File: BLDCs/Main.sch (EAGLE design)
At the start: 60 parts, among them IC1 MEGA8-AI, IC3 TP4056, J1 PIC_ICSP_MINI_5_PIN, U4 LM1117 3.3, X1 MINI-USB-32005-201, Y1 16MHZ

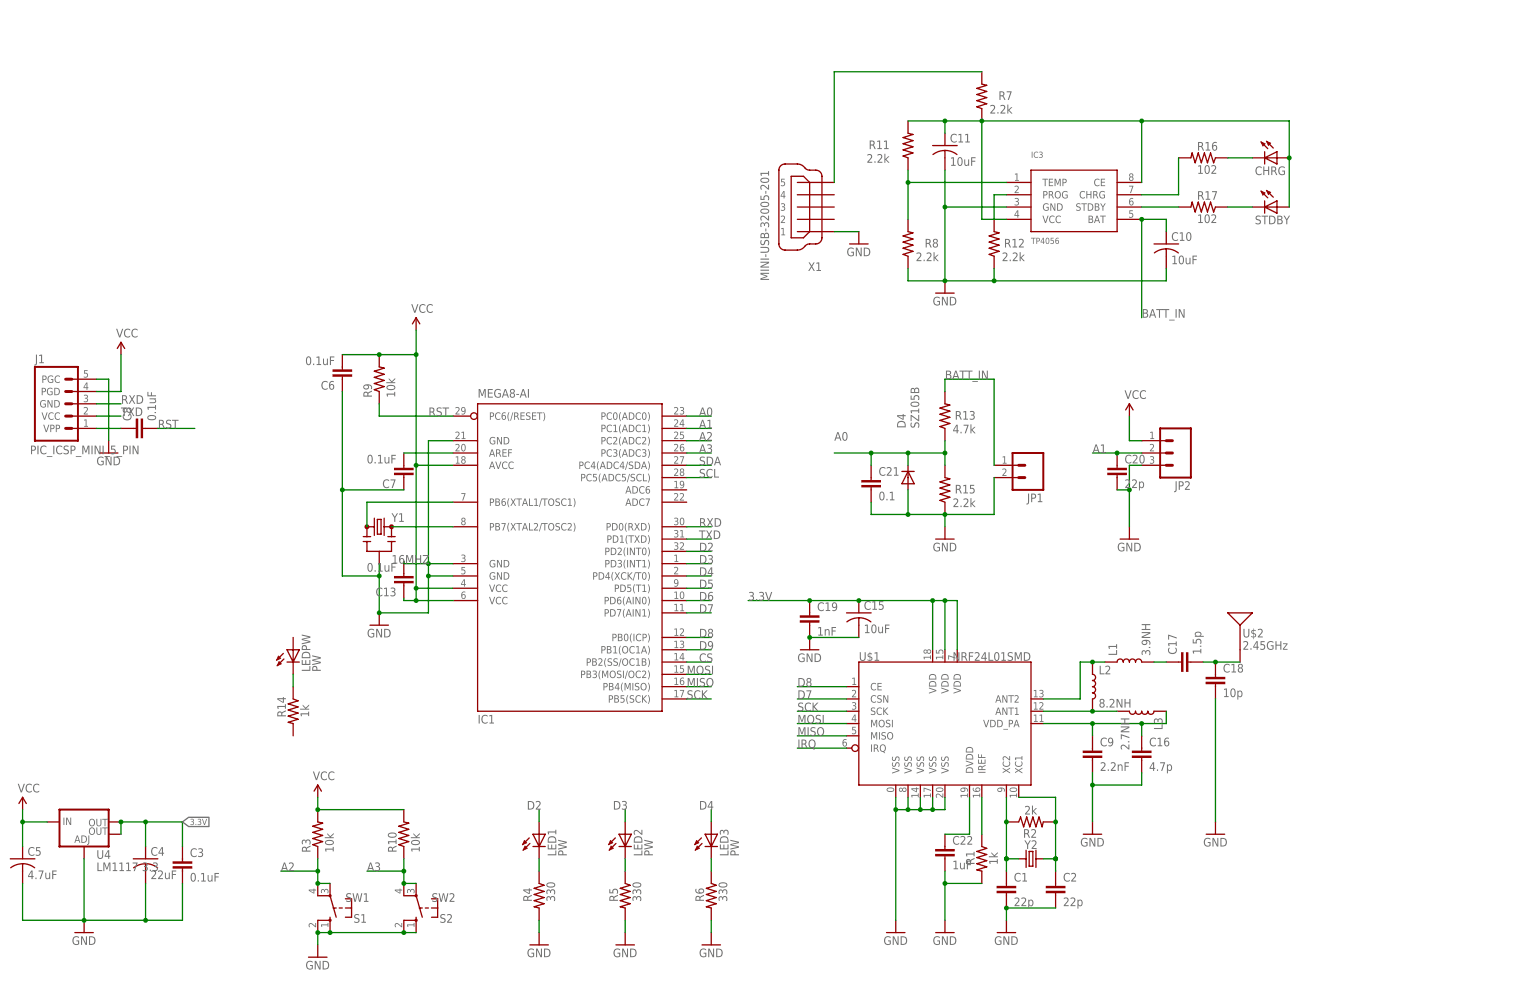
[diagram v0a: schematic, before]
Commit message: add license
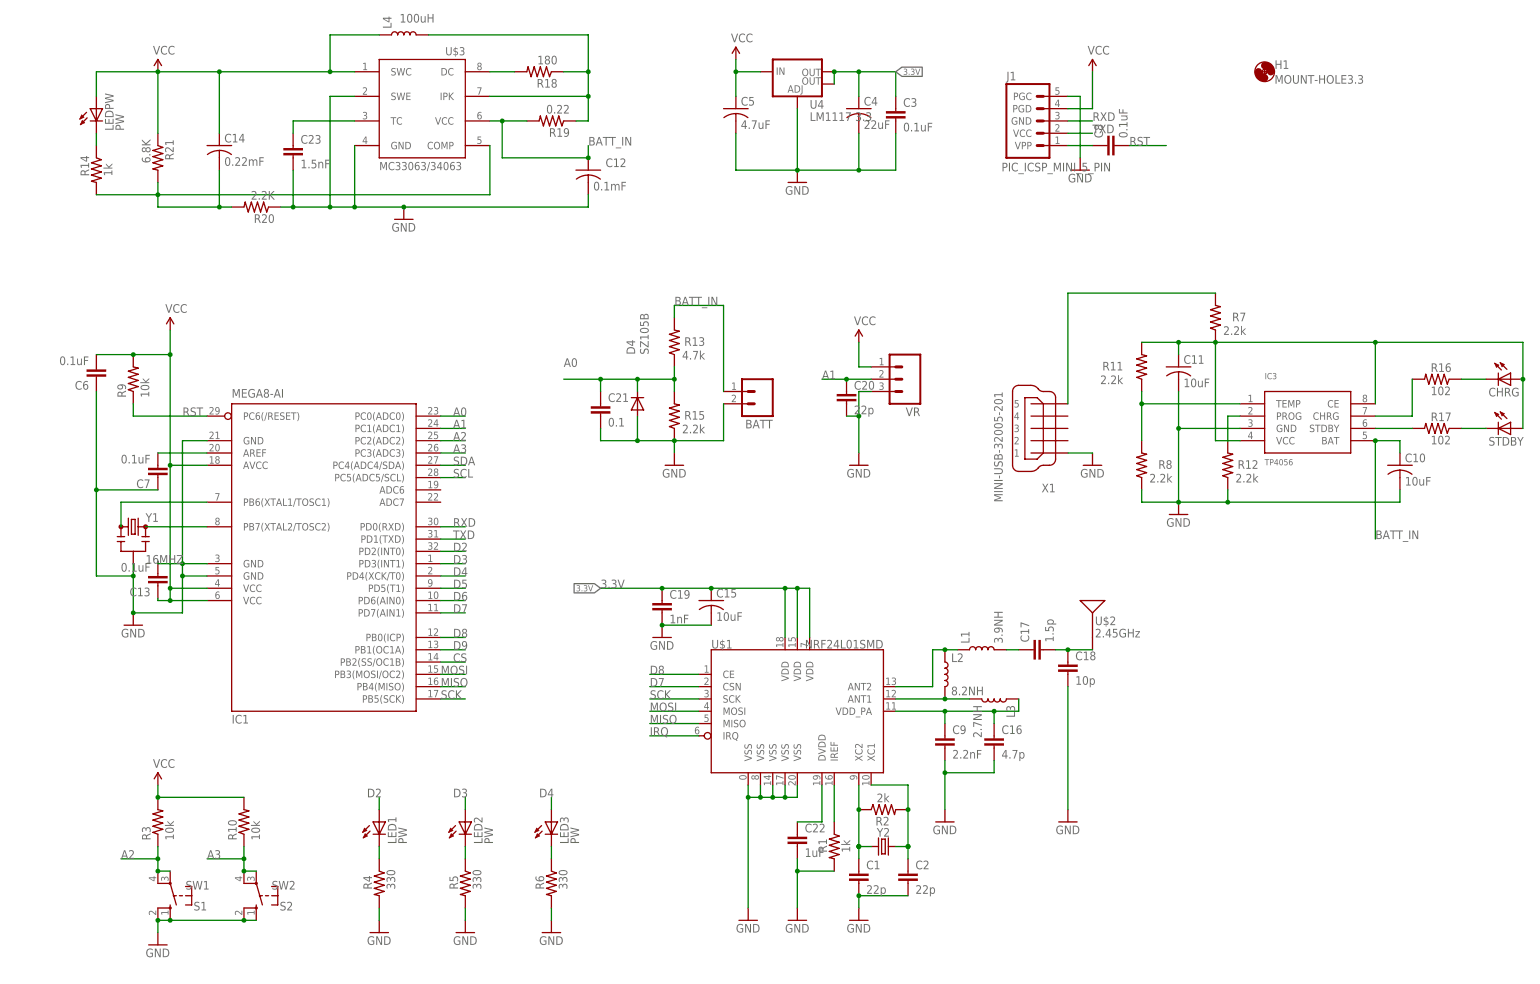
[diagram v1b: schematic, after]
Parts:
- removed JP1: (no value), SparkFun:M02LOCK
- removed JP2: (no value), SparkFun:M03LOCK
- added BATT: (no value), SparkFun:M02LOCK
- added C12: 0.1mF, adafruit:C-USC1206
- added C14: 0.22mF, adafruit:C-USC1206
- added C23: 1.5nF, SparkFun-Passives:CAP0805
- added H1: MOUNT-HOLE3.3, holes:MOUNT-HOLE3.3
- added L4: 100uH, SparkFun-Coils:INDUCTOR-0402-3.9NH
- added R18: 180, SparkFun-Resistors:RESISTOR0805-RES
- added R19: 0.22, SparkFun-Resistors:RESISTOR0805-RES
- added R20: 2.2K, SparkFun-Resistors:RESISTOR0805-RES
- added R21: 6.8K, SparkFun-Resistors:RESISTOR0805-RES
- added U$3: MC33063/MC34063D, adafruit:MC33063/MC34063D
- added VR: (no value), SparkFun:M03LOCK
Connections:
- new net N$26: C14.2, R14.2, R20.2, R21.2, U$3.COMP
- new net N$28: C23.1, U$3.TC
- new net N$34: R18.2, U$3.DC
- new net N$35: L4.2, R18.1, R19.1, U$3.IPK
- net A1: now also VR.2; no longer JP2.2
- net BATT_IN: now also BATT.1, C12.1, R19.2, U$3.VCC; no longer JP1.1
- net GND: now also BATT.2, C12.2, C23.2, R20.1, U$3.GND, U$3.SWE, VR.3; no longer JP1.2, JP2.3
- net VCC: now also C14.1, L4.1, LEDPW.A, R21.1, U$3.SWC, VR.1; no longer JP2.1
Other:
- moved on the sheet: C1, C10, C11, C13, C15, C16, C17, C18, C19, C2, C20, C21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
